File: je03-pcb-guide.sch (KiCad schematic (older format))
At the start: 1 part

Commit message: Add components
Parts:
- added C?: 1uF, symbol Device:C_Small
- added C? (x3): 0.1uF, symbol Device:C_Small
- added C?: 10uF, symbol Device:C_Small
- added C? (x2): 22pF, symbol Device:C_Small
- added R? (x2): 10k, symbol Device:R_Small
- added R? (x2): 22 ohm, symbol Device:R_Small
- added SW?: SW_Push, symbol Switch:SW_Push
- added Y?: 16MHz, symbol Device:Crystal_GND24_Small
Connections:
- net +5V: now also U?.7 (VBUS), C?.1, C?.1, C?.1, C?.1, R?.1
- net GND: now also C?.2, C?.2, C?.2, C?.2, C?.2, C?.2, C?.2, R?.1, SW?.1, Y?.2, Y?.4
- net at U?.13 (~RESET): now also R?.2, SW?.2
- net at U?.16 (XTAL2): now also C?.1, Y?.3
- net at U?.17 (XTAL1): now also C?.1, Y?.1
- net at U?.3 (D-): now also R?.1
- net at U?.33 (~HWB~/PE2): now also R?.2
- net at U?.4 (D+): now also R?.1
- net at U?.6 (UCAP): now also C?.1
- new net D+: R?.2
- new net D-: R?.2

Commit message: Assign components
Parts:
- added D1, D2, D3, D4: SOD-123, Diode_SMD:D_SOD-123, symbol Device:D_Small
- added F1: 500mA, Fuse:Fuse_1206_3216Metric, symbol Device:Polyfuse_Small
- added MX1, MX2, MX3, MX4: MX-NoLED, MX_Alps_Hybrid:MX-1U-NoLED, symbol MX_Alps_Hybrid:MX-NoLED
- added USB1: Molex-0548190589, random-keyboard-parts:Molex-0548190589, symbol random-keyboard-parts:Molex-0548190589
- C1, C2, C3, C4, C5, C6, C7: renamed from C?; footprint (none) -> Capacitor_SMD:C_0805_2012Metric
- R1, R2, R3, R4: renamed from R?; footprint (none) -> Resistor_SMD:R_0805_2012Metric
- SW1: renamed from SW?; footprint (none) -> random-keyboard-parts:SKQG-1155865
- Y1: renamed from Y?; footprint (none) -> Crystal:Crystal_SMD_3225-4Pin_3.2x2.5mm
- gave numbers to parts that had none: 1
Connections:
- net +5V: now also F1.1
- net D+: now also USB1.3 (D+)
- net D-: now also USB1.4 (D-)
- net GND: now also USB1.1 (GND)
- net ROW0: now reaches U1.27 (PD7)
- net ROW0: now also D1.1 (K), D2.1 (K)
- net COL1: now reaches U1.28 (PB4)
- net COL1: now also MX2.1 (COL), MX4.1 (COL)
- net COL0: now reaches U1.29 (PB5)
- net COL0: now also MX1.1 (COL), MX3.1 (COL)
- net ROW1: now reaches U1.30 (PB6)
- net ROW1: now also D3.1 (K), D4.1 (K)
- new net: D1.2 (A), MX1.2 (ROW)
- new net: D2.2 (A), MX2.2 (ROW)
- new net: D3.2 (A), MX3.2 (ROW)
- new net: D4.2 (A), MX4.2 (ROW)
- new net VCC: F1.2, USB1.5 (VBUS)
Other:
- moved on the sheet: R4

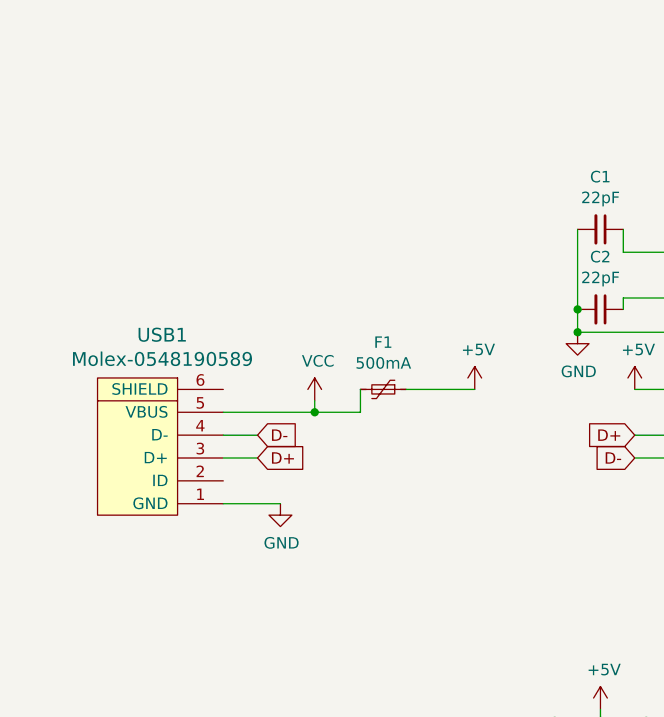
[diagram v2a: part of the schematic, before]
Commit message: Add USB-C
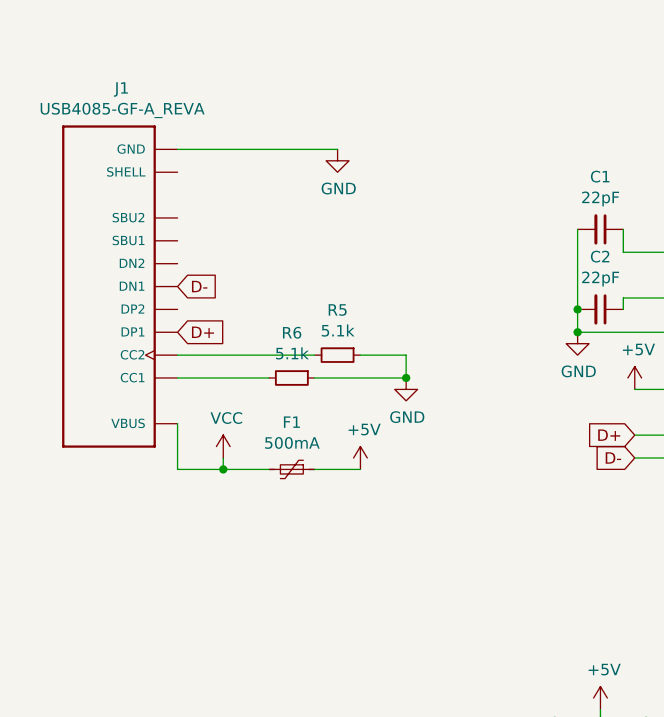
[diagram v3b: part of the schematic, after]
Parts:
- removed USB1: Molex-0548190589, random-keyboard-parts:Molex-0548190589, symbol random-keyboard-parts:Molex-0548190589
- added J1: USB4085-GF-A_REVA, USB4085-GF-A_REVA:GCT_USB4085-GF-A_REVA, symbol USB4085-GF-A_REVA:USB4085-GF-A_REVA
- added R5, R6: 5.1k, Resistor_SMD:R_0603_1608Metric, symbol Device:R_Small
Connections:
- net D+: now also J1.A6 (DP1)
- net D-: now also J1.A7 (DN1)
- net GND: now also J1.A1 (GND), J1.A12 (GND), J1.B1 (GND), J1.B12 (GND), R5.1, R6.1
- net VCC: now also J1.A4 (VBUS), J1.A9 (VBUS), J1.B4 (VBUS), J1.B9 (VBUS)
- new net: J1.B5 (CC2), R5.2
- new net: J1.A5 (CC1), R6.2
- new net: J1.P1 (SHELL), J1.P2 (SHELL), J1.P3 (SHELL), J1.P4 (SHELL)
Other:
- moved on the sheet: F1
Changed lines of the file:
@@
-$EndComp
-$Comp
-L Device:C_Small C4
-U 1 1 5F4BBF4B
-P 3550 4200
-F 0 "C4" H 3642 4246 50  0000 L CNN
-F 1 "0.1uF" H 3642 4155 50  0000 L CNN
-F 2 "Capacitor_SMD:C_0805_2012Metric" H 3550 4200 50  0001 C CNN
-F 3 "~" H 3550 4200 50  0001 C CNN
-	1    3550 4200
-	1    0    0    -1
 $EndComp
 $Comp
@@
 	1    0    0    -1
 $EndComp
-Wire Wire Line
-	3550 4100 3950 4100
-Connection ~ 3950 4100
 Connection ~ 4350 4100
 Wire Wire Line
@@
 Text GLabel 4300 2950 0    50   Input ~ 0
 D-
-$Comp
-L random-keyboard-parts:Molex-0548190589 USB1
-U 1 1 5F4E16D9
-P 2200 2950
-F 0 "USB1" V 2737 2917 60  0000 C CNN
-F 1 "Molex-0548190589" V 2631 2917 60  0000 C CNN
-F 2 "random-keyboard-parts:Molex-0548190589" H 2200 2950 60  0001 C CNN
-F 3 "" H 2200 2950 60  0001 C CNN
-	1    2200 2950
-	0    -1   -1   0
-$EndComp
-Text GLabel 2650 2950 2    50   Input ~ 0
-D+
-Text GLabel 2650 2850 2    50   Input ~ 0
-D-
-$Comp
-L power:GND #PWR0111
-U 1 1 5F4E5482
-P 2750 3150
-F 0 "#PWR0111" H 2750 2900 50  0001 C CNN
-F 1 "GND" H 2755 2977 50  0000 C CNN
-F 2 "" H 2750 3150 50  0001 C CNN
-F 3 "" H 2750 3150 50  0001 C CNN
-	1    2750 3150
-	1    0    0    -1
-$EndComp
-Wire Wire Line
-	2750 3150 2500 3150
-$Comp
-L Device:Polyfuse_Small F1
-U 1 1 5F4E6A99
-P 3200 2650
-F 0 "F1" V 2995 2650 50  0000 C CNN
-F 1 "500mA" V 3086 2650 50  0000 C CNN
-F 2 "Fuse:Fuse_1206_3216Metric" H 3250 2450 50  0001 L CNN
-F 3 "~" H 3200 2650 50  0001 C CNN
-	1    3200 2650
-	0    1    1    0
-$EndComp
-$Comp
-L power:+5V #PWR0112
-U 1 1 5F4E7B01
-P 3600 2650
-F 0 "#PWR0112" H 3600 2500 50  0001 C CNN
-F 1 "+5V" H 3615 2823 50  0000 C CNN
-F 2 "" H 3600 2650 50  0001 C CNN
-F 3 "" H 3600 2650 50  0001 C CNN
-	1    3600 2650
-	1    0    0    -1
-$EndComp
-Wire Wire Line
-	3600 2650 3300 2650
-Wire Wire Line
-	2650 2850 2500 2850
-Wire Wire Line
-	2500 2950 2650 2950
-Wire Wire Line
-	3100 2650 3100 2750
-Wire Wire Line
-	3100 2750 2900 2750
-$Comp
-L power:VCC #PWR0113
-U 1 1 5F4F2DA6
-P 2900 2700
-F 0 "#PWR0113" H 2900 2550 50  0001 C CNN
-F 1 "VCC" H 2915 2873 50  0000 C CNN
-F 2 "" H 2900 2700 50  0001 C CNN
-F 3 "" H 2900 2700 50  0001 C CNN
-	1    2900 2700
-	1    0    0    -1
-$EndComp
-Wire Wire Line
-	2900 2700 2900 2750
-Connection ~ 2900 2750
-Wire Wire Line
-	2900 2750 2500 2750
 $Comp
 L MX_Alps_Hybrid:MX-NoLED MX1
@@
 Text GLabel 6350 3750 2    50   Input ~ 0
 ROW0
+Connection ~ 3950 4100
+Wire Wire Line
+	2500 3000 2700 3000
+Connection ~ 2500 3000
+Wire Wire Line
+	2500 2950 2500 3000
+Wire Wire Line
+	2900 3000 3100 3000
+$Comp
+L power:VCC #PWR0113
+U 1 1 5F4F2DA6
+P 2500 2950
+F 0 "#PWR0113" H 2500 2800 50  0001 C CNN
+F 1 "VCC" H 2515 3123 50  0000 C CNN
+F 2 "" H 2500 2950 50  0001 C CNN
+F 3 "" H 2500 2950 50  0001 C CNN
+	1    2500 2950
+	1    0    0    -1
+$EndComp
+$Comp
+L power:+5V #PWR0112
+U 1 1 5F4E7B01
+P 3100 3000
+F 0 "#PWR0112" H 3100 2850 50  0001 C CNN
+F 1 "+5V" H 3115 3173 50  0000 C CNN
+F 2 "" H 3100 3000 50  0001 C CNN
+F 3 "" H 3100 3000 50  0001 C CNN
+	1    3100 3000
+	1    0    0    -1
+$EndComp
+$Comp
+L Device:Polyfuse_Small F1
+U 1 1 5F4E6A99
+P 2800 3000
+F 0 "F1" V 2595 3000 50  0000 C CNN
+F 1 "500mA" V 2686 3000 50  0000 C CNN
+F 2 "Fuse:Fuse_1206_3216Metric" H 2850 2800 50  0001 L CNN
+F 3 "~" H 2800 3000 50  0001 C CNN
+	1    2800 3000
+	0    1    1    0
+$EndComp
+Wire Wire Line
+	3550 4100 3950 4100
+$Comp
+L Device:C_Small C4
+U 1 1 5F4BBF4B
+P 3550 4200
+F 0 "C4" H 3642 4246 50  0000 L CNN
+F 1 "0.1uF" H 3642 4155 50  0000 L CNN
+F 2 "Capacitor_SMD:C_0805_2012Metric" H 3550 4200 50  0001 C CNN
+F 3 "~" H 3550 4200 50  0001 C CNN
+	1    3550 4200
+	1    0    0    -1
+$EndComp
+$Comp
+L Device:R_Small R5
+U 1 1 5F4C4BED
+P 3000 2500
+F 0 "R5" V 2804 2500 50  0000 C CNN
+F 1 "5.1k" V 2895 2500 50  0000 C CNN
+F 2 "Resistor_SMD:R_0603_1608Metric" H 3000 2500 50  0001 C CNN
+F 3 "~" H 3000 2500 50  0001 C CNN
+	1    3000 2500
+	0    1    1    0
+$EndComp
+$Comp
+L power:GND #PWR0114
+U 1 1 5F4D2639
+P 3300 2600
+F 0 "#PWR0114" H 3300 2350 50  0001 C CNN
+F 1 "GND" H 3305 2427 50  0000 C CNN
+F 2 "" H 3300 2600 50  0001 C CNN
+F 3 "" H 3300 2600 50  0001 C CNN
+	1    3300 2600
+	1    0    0    -1
+$EndComp
+$Comp
+L USB4085-GF-A_REVA:USB4085-GF-A_REVA J1
+U 1 1 5F4D58DE
+P 2000 2200
+F 0 "J1" H 1943 1333 50  0000 C CNN
+F 1 "USB4085-GF-A_REVA" H 1943 1424 50  0000 C CNN
+F 2 "USB4085-GF-A_REVA:GCT_USB4085-GF-A_REVA" H 2000 2200 50  0001 L BNN
+F 3 "Manufacturer Recommendations" H 2000 2200 50  0001 L BNN
+F 4 "A" H 2000 2200 50  0001 L BNN "Field4"
+F 5 "Global Connector Technology" H 2000 2200 50  0001 L BNN "Field5"
+	1    2000 2200
+	-1   0    0    1
+$EndComp
+Wire Wire Line
+	2300 3000 2300 2800
+Wire Wire Line
+	2300 3000 2500 3000
+Wire Wire Line
+	2300 2500 2900 2500
+Text GLabel 2300 2200 2    50   Input ~ 0
+D-
+Text GLabel 2300 2400 2    50   Input ~ 0
+D+
+$Comp
+L power:GND #PWR0111
+U 1 1 5F4E5482
+P 3000 1600
+F 0 "#PWR0111" H 3000 1350 50  0001 C CNN
+F 1 "GND" H 3005 1427 50  0000 C CNN
+F 2 "" H 3000 1600 50  0001 C CNN
+F 3 "" H 3000 1600 50  0001 C CNN
+	1    3000 1600
+	1    0    0    -1
+$EndComp
+Wire Wire Line
+	3000 1600 2300 1600
+$Comp
+L Device:R_Small R6
+U 1 1 5F4E7538
+P 2800 2600
+F 0 "R6" V 2604 2600 50  0000 C CNN
+F 1 "5.1k" V 2695 2600 50  0000 C CNN
+F 2 "Resistor_SMD:R_0603_1608Metric" H 2800 2600 50  0001 C CNN
+F 3 "~" H 2800 2600 50  0001 C CNN
+	1    2800 2600
+	0    1    1    0
+$EndComp
+Wire Wire Line
+	3300 2500 3300 2600
+Wire Wire Line
+	3100 2500 3300 2500
+Wire Wire Line
+	2900 2600 3300 2600
+Connection ~ 3300 2600
+Wire Wire Line
+	2700 2600 2300 2600
 $EndSCHEMATC

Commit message: USB-C
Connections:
- net GND: now also J1.P1 (SHELL), J1.P2 (SHELL), J1.P3 (SHELL), J1.P4 (SHELL)
- no-connect marks 0 -> 5
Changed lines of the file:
@@
 U 1 1 5F4C4BED
 P 3000 2500
-F 0 "R5" V 2804 2500 50  0000 C CNN
-F 1 "5.1k" V 2895 2500 50  0000 C CNN
+F 0 "R5" V 2900 2500 50  0000 C CNN
+F 1 "5.1k" V 3000 2500 50  0000 C CNN
 F 2 "Resistor_SMD:R_0603_1608Metric" H 3000 2500 50  0001 C CNN
 F 3 "~" H 3000 2500 50  0001 C CNN
@@
 	1    3300 2600
 	1    0    0    -1
-$EndComp
-$Comp
-L USB4085-GF-A_REVA:USB4085-GF-A_REVA J1
-U 1 1 5F4D58DE
-P 2000 2200
-F 0 "J1" H 1943 1333 50  0000 C CNN
-F 1 "USB4085-GF-A_REVA" H 1943 1424 50  0000 C CNN
-F 2 "USB4085-GF-A_REVA:GCT_USB4085-GF-A_REVA" H 2000 2200 50  0001 L BNN
-F 3 "Manufacturer Recommendations" H 2000 2200 50  0001 L BNN
-F 4 "A" H 2000 2200 50  0001 L BNN "Field4"
-F 5 "Global Connector Technology" H 2000 2200 50  0001 L BNN "Field5"
-	1    2000 2200
-	-1   0    0    1
 $EndComp
 Wire Wire Line
@@
 $EndComp
 Wire Wire Line
-	3000 1600 2300 1600
+	3000 1600 2400 1600
 $Comp
 L Device:R_Small R6
 U 1 1 5F4E7538
 P 2800 2600
-F 0 "R6" V 2604 2600 50  0000 C CNN
-F 1 "5.1k" V 2695 2600 50  0000 C CNN
+F 0 "R6" V 2700 2600 50  0000 C CNN
+F 1 "5.1k" V 2800 2600 50  0000 C CNN
 F 2 "Resistor_SMD:R_0603_1608Metric" H 2800 2600 50  0001 C CNN
 F 3 "~" H 2800 2600 50  0001 C CNN
@@
 Wire Wire Line
 	2700 2600 2300 2600
+NoConn ~ 2300 1900
+NoConn ~ 2300 2000
+Wire Wire Line
+	2300 1700 2400 1700
+Wire Wire Line
+	2400 1700 2400 1600
+Connection ~ 2400 1600
+Wire Wire Line
+	2400 1600 2300 1600
+$Comp
+L USB4085-GF-A_REVA:USB4085-GF-A_REVA J1
+U 1 1 5F4D58DE
+P 2000 2200
+F 0 "J1" H 1943 1333 50  0000 C CNN
+F 1 "USB4085-GF-A_REVA" H 1943 1424 50  0000 C CNN
+F 2 "USB4085-GF-A_REVA:GCT_USB4085-GF-A_REVA" H 2000 2200 50  0001 L BNN
+F 3 "Manufacturer Recommendations" H 2000 2200 50  0001 L BNN
+F 4 "A" H 2000 2200 50  0001 L BNN "Field4"
+F 5 "Global Connector Technology" H 2000 2200 50  0001 L BNN "Field5"
+	1    2000 2200
+	-1   0    0    1
+$EndComp
+NoConn ~ 2300 2300
+NoConn ~ 2300 2100
+NoConn ~ 3100 -600
 $EndSCHEMATC

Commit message: Misc
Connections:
- net D+: now also J1.B6 (DP2)
- net D-: now also J1.B7 (DN2)
- no-connect marks 5 -> 3
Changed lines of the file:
@@
 Wire Wire Line
 	2300 2500 2900 2500
-Text GLabel 2300 2200 2    50   Input ~ 0
+Text GLabel 2400 2150 2    50   Input ~ 0
 D-
-Text GLabel 2300 2400 2    50   Input ~ 0
+Text GLabel 2400 2350 2    50   Input ~ 0
 D+
 $Comp
@@
 	-1   0    0    1
 $EndComp
-NoConn ~ 2300 2300
-NoConn ~ 2300 2100
 NoConn ~ 3100 -600
+Wire Wire Line
+	2300 2100 2400 2100
+Wire Wire Line
+	2300 2200 2400 2200
+Wire Wire Line
+	2400 2100 2400 2200
+Wire Wire Line
+	2300 2400 2400 2400
+Wire Wire Line
+	2300 2300 2400 2300
+Wire Wire Line
+	2400 2300 2400 2400
 $EndSCHEMATC
